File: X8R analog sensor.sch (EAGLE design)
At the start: 15 parts, among them IC1 MCP1703CB, U1 ATTINY13SOIC

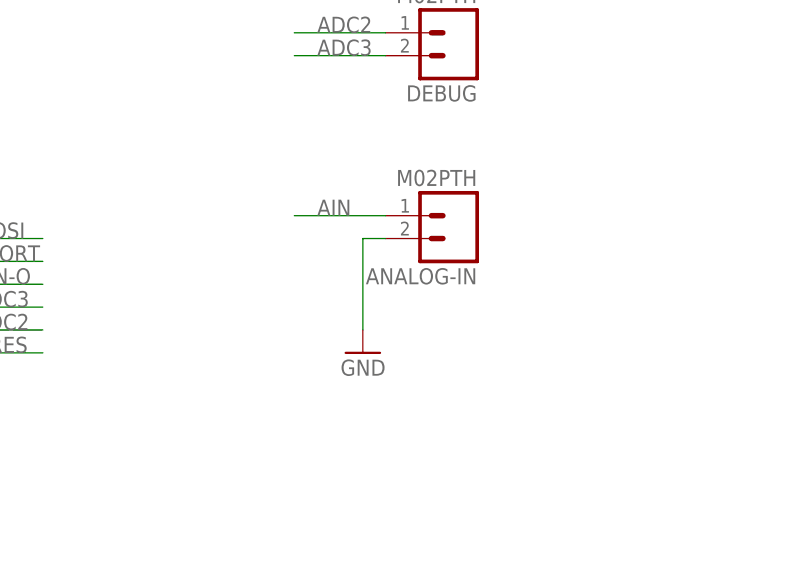
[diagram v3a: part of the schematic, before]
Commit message: reverted back to the 3 pin connector on AIN
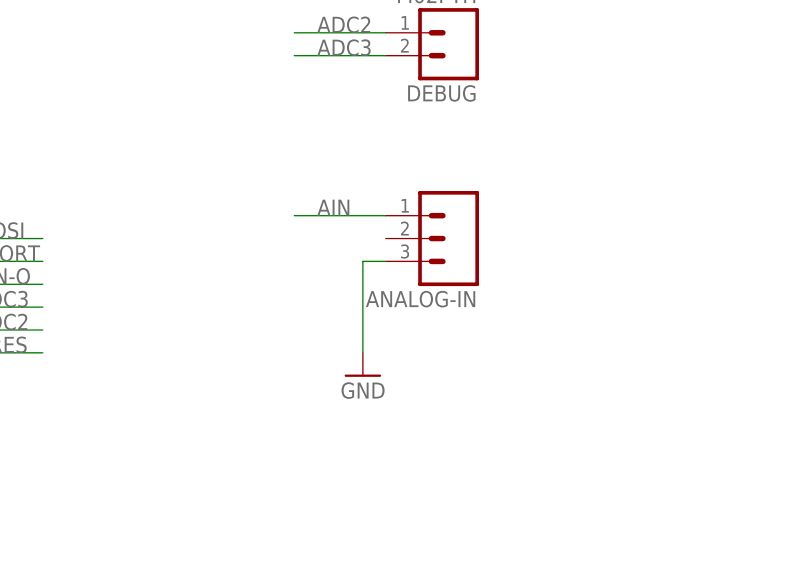
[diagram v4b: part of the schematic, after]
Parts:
- ANALOG-IN: value M02PTH -> (none); device SparkFun-Connectors:M02PTH -> SparkFun-Connectors:M03PTH
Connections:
- net GND: now also ANALOG-IN.3; no longer ANALOG-IN.2
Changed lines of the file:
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@@
 <part name="GND6" library="SparkFun-Aesthetics" deviceset="GND" device=""/>
 <part name="C4" library="SparkFun-Capacitors" deviceset="CAP" device="0603-CAP" value=".1uf"/>
-<part name="ANALOG-IN" library="SparkFun-Connectors" deviceset="M02" device="PTH"/>
+<part name="ANALOG-IN" library="SparkFun-Connectors" deviceset="M03" device="PTH"/>
 </parts>
 <sheets>
@@
 <instance part="GND1" gate="1" x="66.04" y="66.04"/>
 <instance part="GND2" gate="1" x="81.28" y="96.52"/>
-<instance part="GND3" gate="1" x="177.8" y="66.04" rot="MR0"/>
+<instance part="GND3" gate="1" x="177.8" y="63.5" rot="MR0"/>
 <instance part="GND4" gate="1" x="99.06" y="60.96"/>
 <instance part="DEBUG" gate="G$1" x="187.96" y="101.6" rot="R180"/>
@@
 <instance part="GND6" gate="1" x="73.66" y="106.68"/>
 <instance part="C4" gate="G$1" x="121.92" y="124.46"/>
-<instance part="ANALOG-IN" gate="G$1" x="187.96" y="81.28" rot="R180"/>
+<instance part="ANALOG-IN" gate="G$1" x="187.96" y="78.74" rot="R180"/>
 </instances>
 <busses>
@@
 <segment>
 <pinref part="GND3" gate="1" pin="GND"/>
-<wire x1="180.34" y1="78.74" x2="177.8" y2="78.74" width="0.1524" layer="91"/>
-<wire x1="177.8" y1="78.74" x2="177.8" y2="68.58" width="0.1524" layer="91"/>
-<pinref part="ANALOG-IN" gate="G$1" pin="2"/>
+<wire x1="180.34" y1="76.2" x2="177.8" y2="76.2" width="0.1524" layer="91"/>
+<wire x1="177.8" y1="76.2" x2="177.8" y2="66.04" width="0.1524" layer="91"/>
+<pinref part="ANALOG-IN" gate="G$1" pin="3"/>
 </segment>
 <segment>

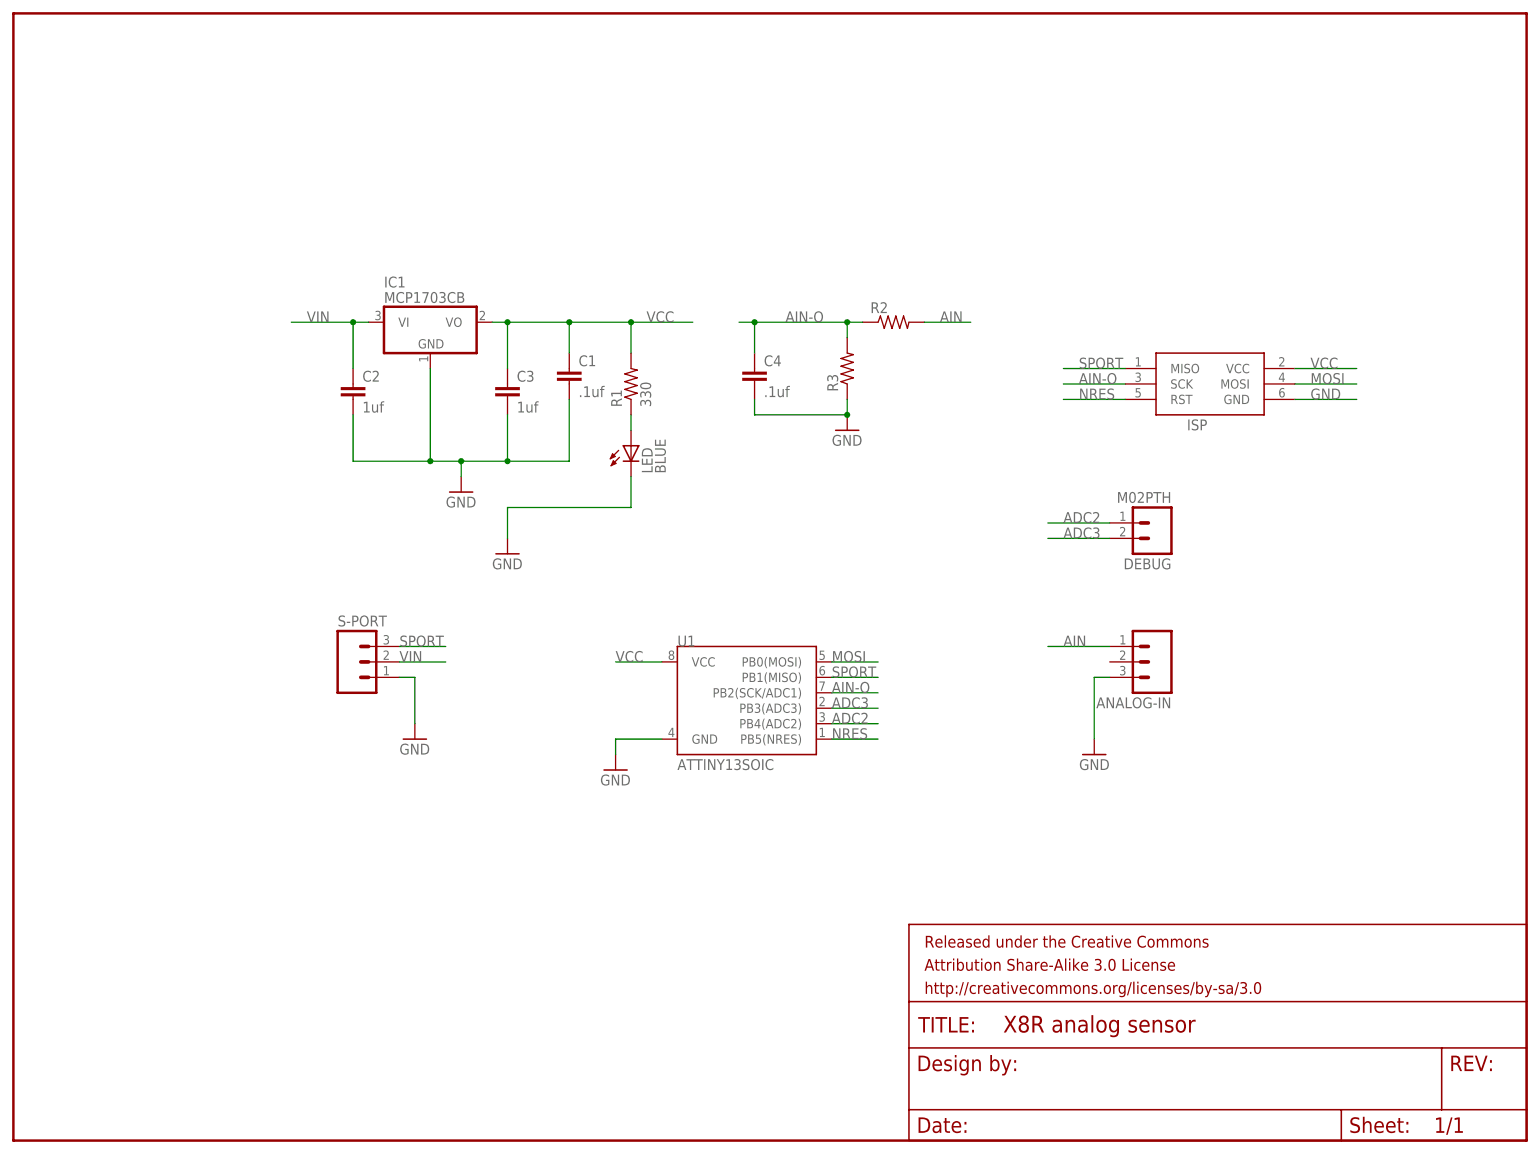
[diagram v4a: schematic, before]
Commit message: updated v2 version with separate grounds
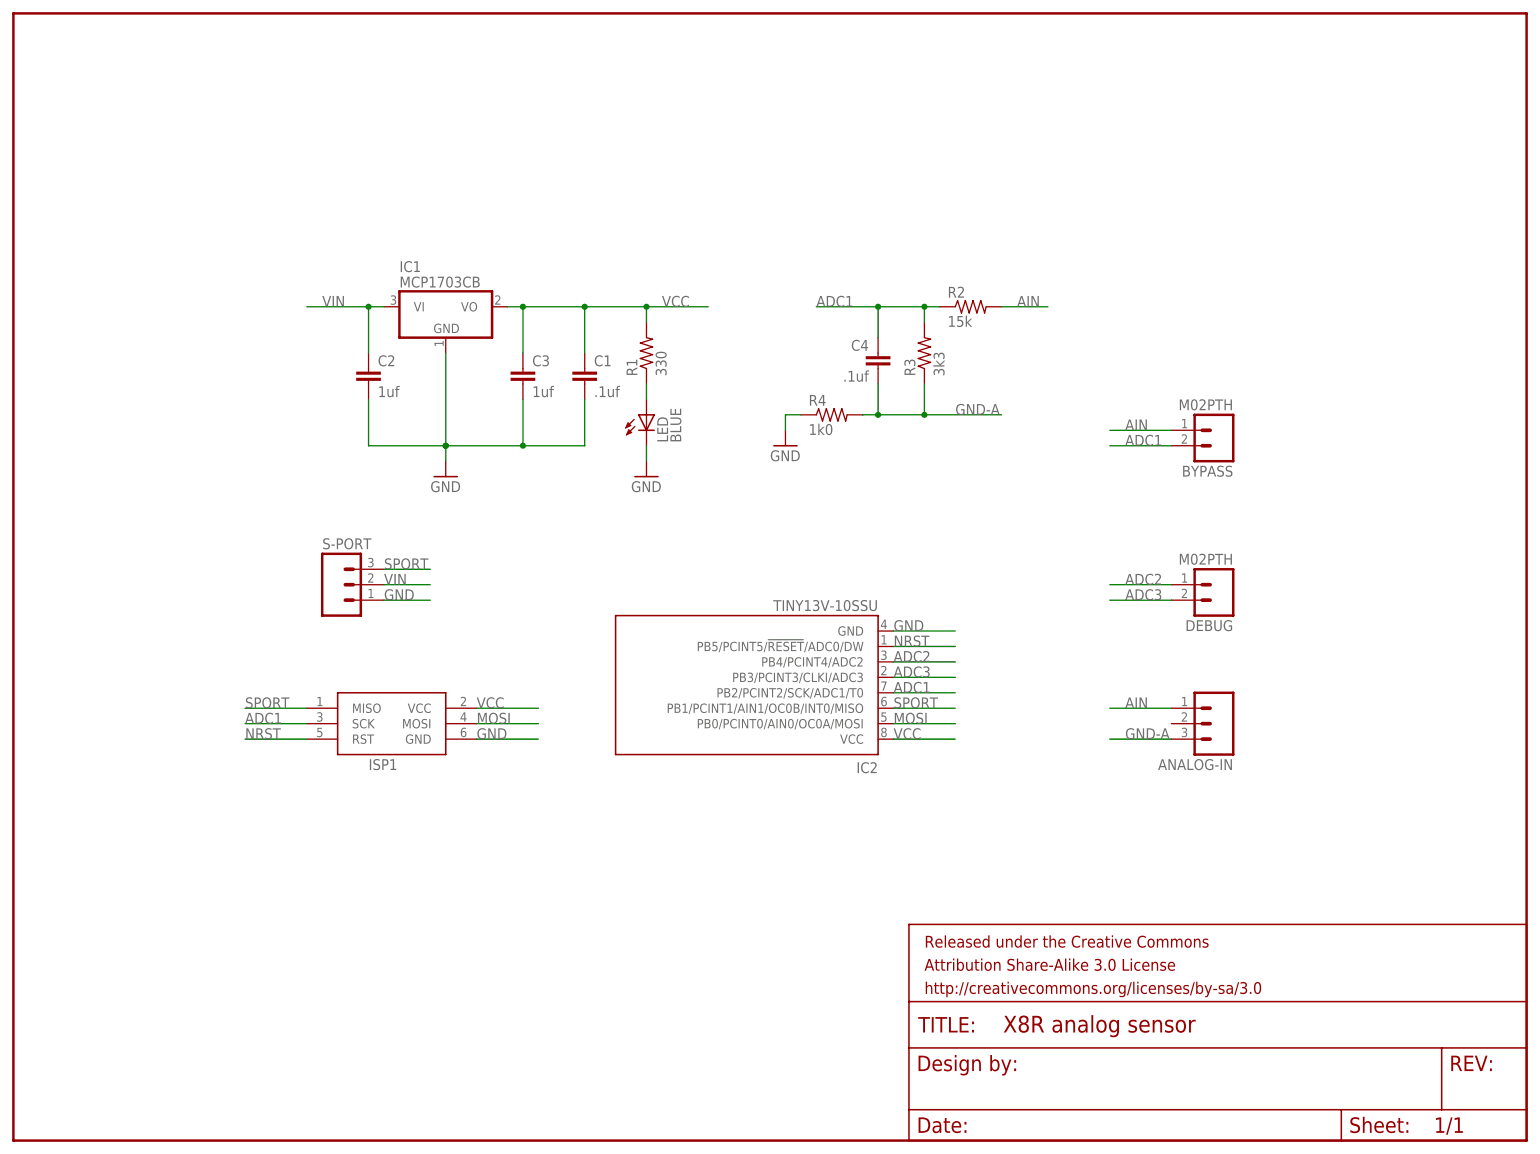
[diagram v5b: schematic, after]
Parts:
- removed ISP: AVRISP-6, adafruit:AVRISP-6
- removed U1: ATTINY13SOIC, SparkFun-DigitalIC:ATTINY13SOIC
- added BYPASS: M02PTH, SparkFun-Connectors:M02PTH
- added IC2: TINY13V-10SSU, atmel:TINY13V-10SSU
- added ISP1: AVRISP-6, adafruit:AVRISP-6
- added R4: 1k0, SparkFun-Resistors:RESISTOR0603
- R2: value (none) -> 15k; device SparkFun-Passives:RESISTORPTH-1/6W -> SparkFun-Passives:RESISTOR0603-RES
- R3: value (none) -> 3k3; device SparkFun-Passives:RESISTORPTH-1/6W -> SparkFun-Passives:RESISTOR0603-RES
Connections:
- removed net AIN-O: C4.1, ISP.SCK, R2.1, R3.2, U1.PB2(SCK/ADC1)
- removed net NRES: ISP.RST, U1.PB5(NRES)
- new net ADC1: BYPASS.2, C4.1, IC2.PB2/PCINT2/SCK/ADC1/T0, ISP1.SCK, R2.1, R3.2
- new net GND-A: ANALOG-IN.3, C4.2, R3.1, R4.2
- new net NRST: IC2.PB5/PCINT5/!RESET!/ADC0/DW, ISP1.RST
- net ADC2: now also IC2.PB4/PCINT4/ADC2; no longer U1.PB4(ADC2)
- net ADC3: now also IC2.PB3/PCINT3/CLKI/ADC3; no longer U1.PB3(ADC3)
- net AIN: now also BYPASS.1
- net GND: now also IC2.GND, ISP1.GND, R4.1; no longer ANALOG-IN.3, C4.2, ISP.GND, R3.1, U1.GND
- net MOSI: now also IC2.PB0/PCINT0/AIN0/OC0A/MOSI, ISP1.MOSI; no longer ISP.MOSI, U1.PB0(MOSI)
- net SPORT: now also IC2.PB1/PCINT1/AIN1/OC0B/INT0/MISO, ISP1.MISO; no longer ISP.MISO, U1.PB1(MISO)
- net VCC: now also IC2.VCC, ISP1.VCC; no longer ISP.VCC, U1.VCC
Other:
- moved on the sheet: ANALOG-IN, C1, C2, C3, C4, DEBUG, IC1, LED, R1, R2, R3, S-PORT
